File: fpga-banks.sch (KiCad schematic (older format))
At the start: 52 parts, among them J13 62000311121, Q12 2N7002, Q13 2N7002, Q14 2N7002, Q15 2N7002, Q16 2N7002, U14 XC7A100T-FGG484

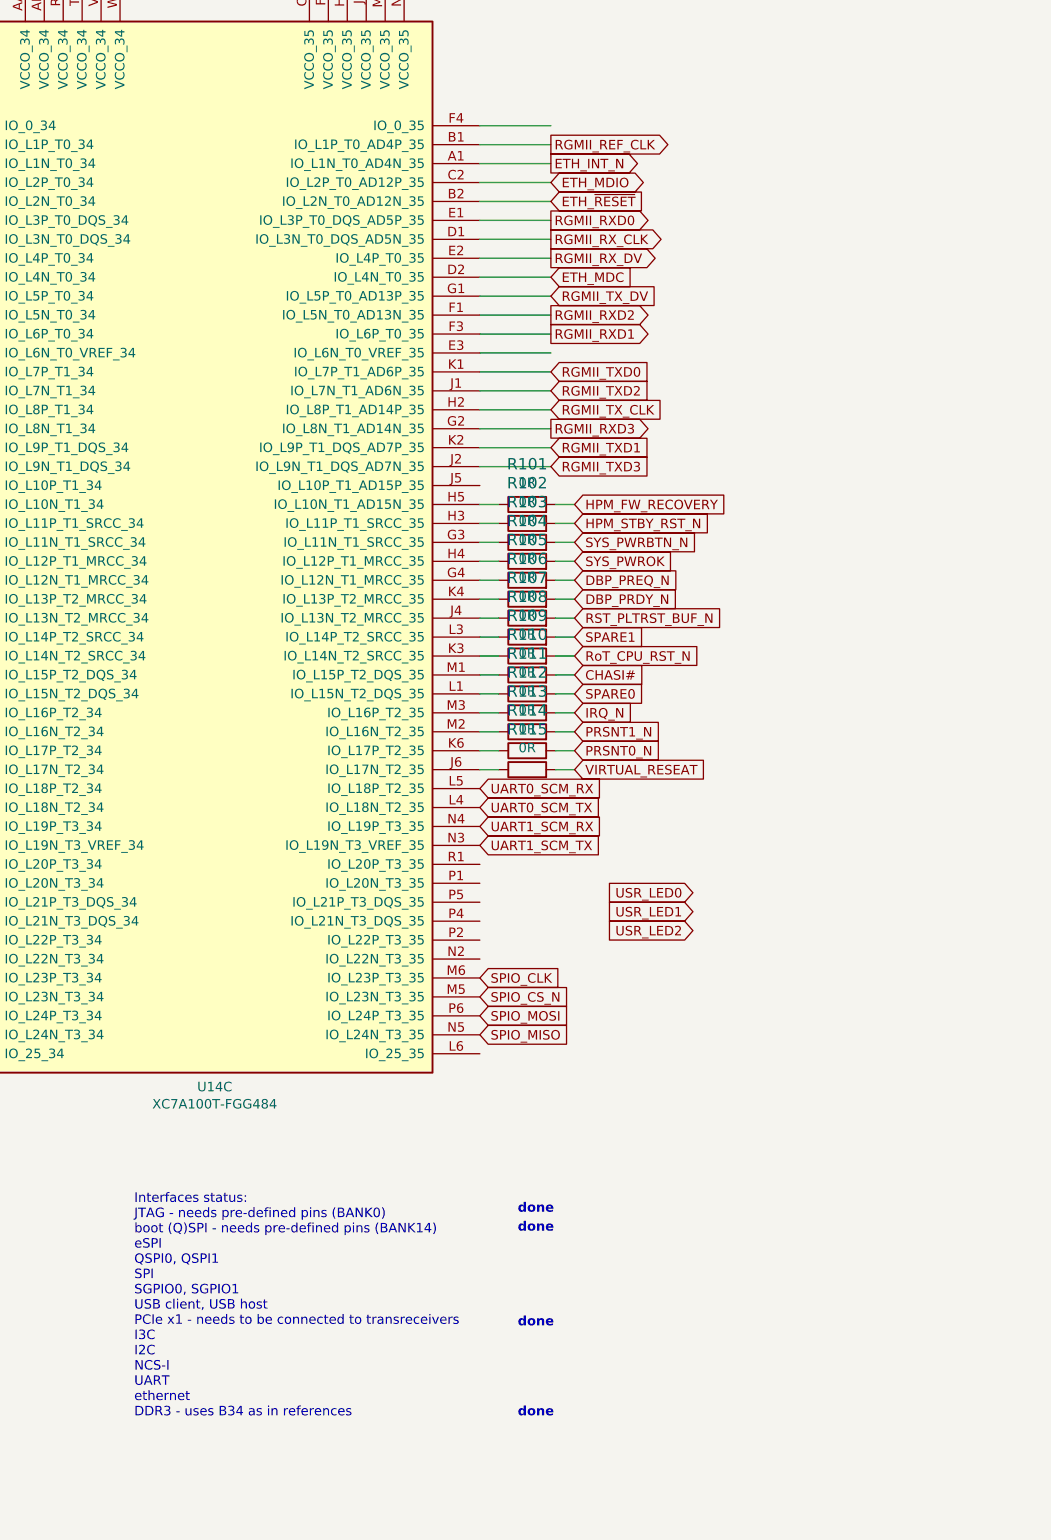
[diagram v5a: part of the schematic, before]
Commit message: Reconnected ethernet
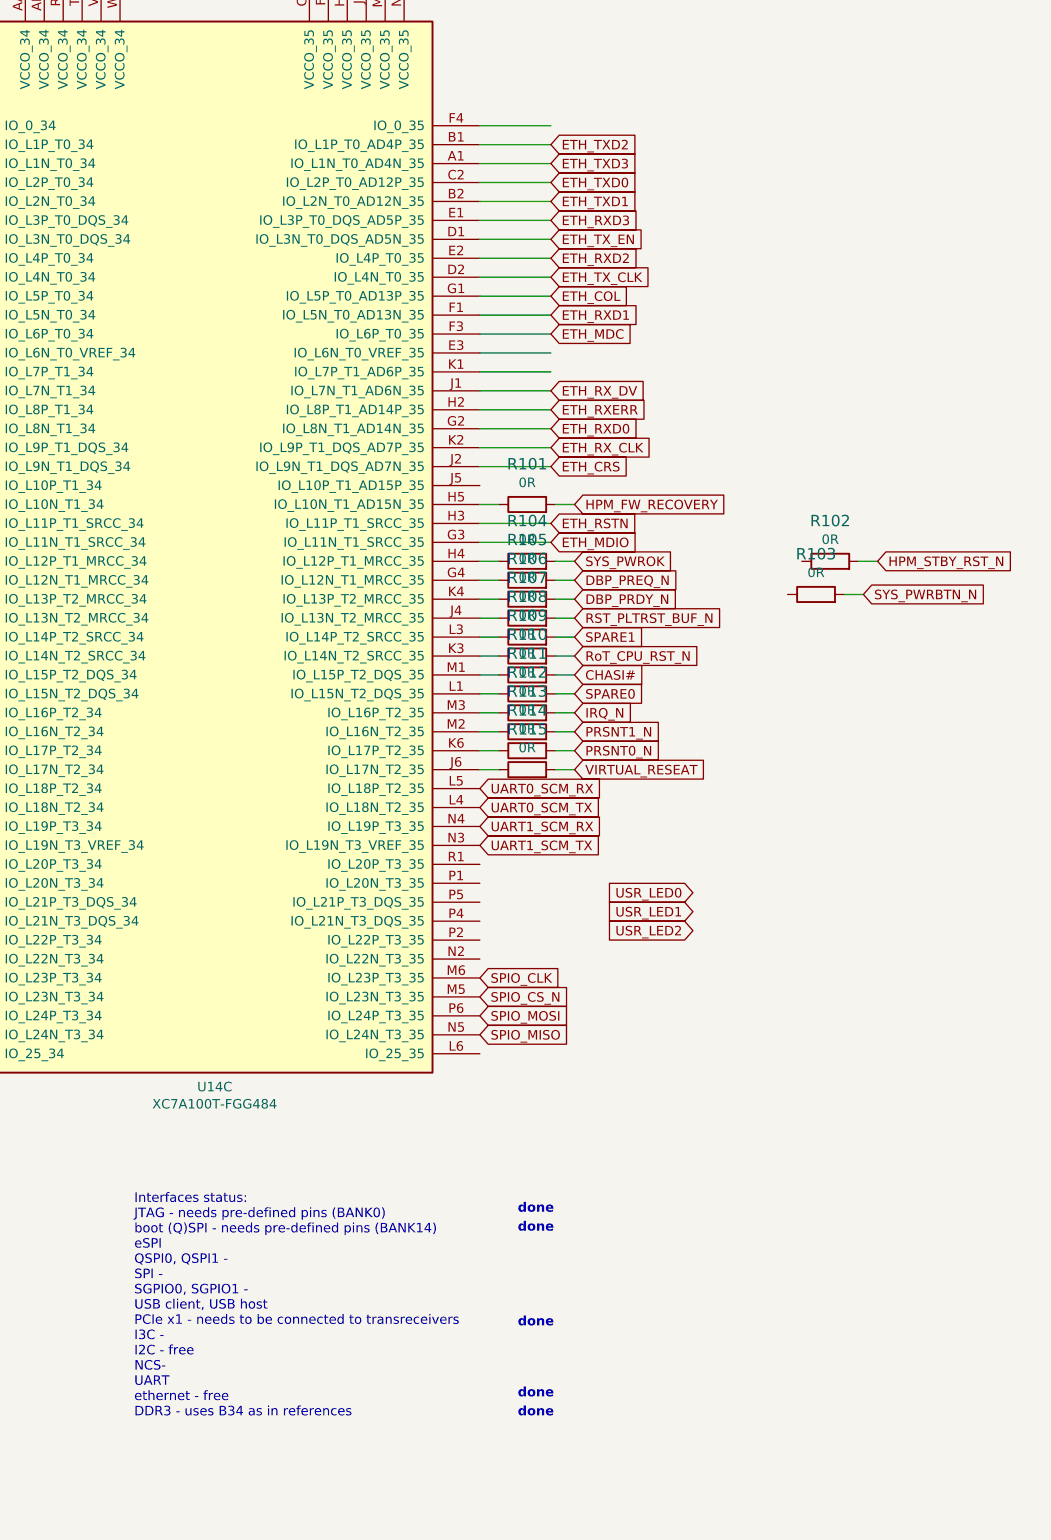
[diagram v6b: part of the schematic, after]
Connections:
- net labels added: ETH_COL, ETH_CRS, ETH_RSTN, ETH_RXD0, ETH_RXD1, ETH_RXD2, ETH_RXD3, ETH_RXERR, ETH_RX_CLK, ETH_RX_DV, ETH_TXD0, ETH_TXD1, ETH_TXD2, ETH_TXD3, ETH_TX_CLK, ETH_TX_EN
- net labels removed: ETH_INT_N, ETH_~RESET, RGMII_REF_CLK, RGMII_RXD0, RGMII_RXD1, RGMII_RXD2, RGMII_RXD3, RGMII_RX_CLK, RGMII_RX_DV, RGMII_TXD0, RGMII_TXD1, RGMII_TXD2, RGMII_TXD3, RGMII_TX_CLK, RGMII_TX_DV
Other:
- note added: "Interfaces status:\nJTAG - needs pre-defined pins (BANK0)\nboot (Q)SPI - needs pre-defined pins (BANK14)\neSPI\nQSPI0, QSPI1 - \nSPI - \nSGPIO0, SGPIO1 - \nUSB client, USB host\nPCIe x1 - needs to be connected to transreceivers\nI3C - \nI2C - free\nNCS-\nUART \nethernet - free\nDDR3 - uses B34 as in references"
- note removed: "Interfaces status:\nJTAG - needs pre-defined pins (BANK0)\nboot (Q)SPI - needs pre-defined pins (BANK14)\neSPI\nQSPI0, QSPI1\nSPI\nSGPIO0, SGPIO1\nUSB client, USB host\nPCIe x1 - needs to be connected to transreceivers\nI3C\nI2C\nNCS-I\nUART\nethernet\nDDR3 - uses B34 as in references"
- moved on the sheet: R102, R103
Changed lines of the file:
@@
 Text GLabel 15300 4000 2    50   Input ~ 0
 HPM_FW_RECOVERY
-Text GLabel 15300 4100 2    50   Input ~ 0
+Text GLabel 16900 4300 2    50   Input ~ 0
 HPM_STBY_RST_N
-Text GLabel 15300 4200 2    50   Input ~ 0
+Text GLabel 16825 4475 2    50   Input ~ 0
 SYS_PWRBTN_N
 Text GLabel 15300 4300 2    50   Input ~ 0
@@
 	0    1    1    0
 $EndComp
-Text GLabel 15175 2400 2    50   Input ~ 0
-ETH_~RESET
-Text GLabel 15175 2200 2    50   Output ~ 0
-ETH_INT_N
-Text GLabel 15175 2100 2    50   Output ~ 0
-RGMII_REF_CLK
-Text GLabel 15175 2300 2    50   BiDi ~ 0
-ETH_MDIO
-Wire Wire Line
-	14800 3800 15175 3800
-Text GLabel 15175 3300 2    50   Input ~ 0
-RGMII_TXD0
-Text GLabel 15175 3700 2    50   Input ~ 0
-RGMII_TXD1
-Text GLabel 15175 3800 2    50   Input ~ 0
-RGMII_TXD3
-Text GLabel 15175 3500 2    50   Input ~ 0
-RGMII_TX_CLK
-Text GLabel 15175 2900 2    50   Input ~ 0
-RGMII_TX_DV
-Text GLabel 15175 3600 2    50   Output ~ 0
-RGMII_RXD3
-Text GLabel 15175 3100 2    50   Output ~ 0
-RGMII_RXD1
-Text GLabel 15175 3400 2    50   Input ~ 0
-RGMII_TXD2
-Text GLabel 15175 3000 2    50   Output ~ 0
-RGMII_RXD2
-Text GLabel 15175 2500 2    50   Output ~ 0
-RGMII_RXD0
-Text GLabel 15175 2700 2    50   Output ~ 0
-RGMII_RX_DV
-Text GLabel 15175 2600 2    50   Output ~ 0
-RGMII_RX_CLK
-Text GLabel 15175 2800 2    50   Input ~ 0
-ETH_MDC
+Wire Wire Line
+	14800 4100 15175 4100
 Wire Wire Line
 	9825 5150 9500 5150
@@
 L artix-dc-scm:R_0R_0402 R102
 U 1 1 61547192
-P 15050 4100
-F 0 "R102" H 15050 4313 60  0000 C CNN
-F 1 "R_0R_0402" H 15050 3950 60  0001 C CNN
-F 2 "artix-dc-scm-footprints:0402-res" H 15250 4300 60  0001 L CNN
-F 3 "" H 15050 4100 50  0001 C CNN
-F 4 "PANASONIC" H 15250 4500 60  0001 L CNN "Manufacturer"
-F 5 "ERJ2GE0R00X" H 15250 4400 60  0001 L CNN "MPN"
-F 6 "0R" H 15050 4215 50  0000 C CNN "Val"
-	1    15050 4100
+P 16650 4300
+F 0 "R102" H 16650 4513 60  0000 C CNN
+F 1 "R_0R_0402" H 16650 4150 60  0001 C CNN
+F 2 "artix-dc-scm-footprints:0402-res" H 16850 4500 60  0001 L CNN
+F 3 "" H 16650 4300 50  0001 C CNN
+F 4 "PANASONIC" H 16850 4700 60  0001 L CNN "Manufacturer"
+F 5 "ERJ2GE0R00X" H 16850 4600 60  0001 L CNN "MPN"
+F 6 "0R" H 16650 4415 50  0000 C CNN "Val"
+	1    16650 4300
 	1    0    0    -1
 $EndComp
@@
 L artix-dc-scm:R_0R_0402 R103
 U 1 1 615497A8
-P 15050 4200
-F 0 "R103" H 15050 4413 60  0000 C CNN
-F 1 "R_0R_0402" H 15050 4050 60  0001 C CNN
-F 2 "artix-dc-scm-footprints:0402-res" H 15250 4400 60  0001 L CNN
-F 3 "" H 15050 4200 50  0001 C CNN
-F 4 "PANASONIC" H 15250 4600 60  0001 L CNN "Manufacturer"
-F 5 "ERJ2GE0R00X" H 15250 4500 60  0001 L CNN "MPN"
-F 6 "0R" H 15050 4315 50  0000 C CNN "Val"
-	1    15050 4200
+P 16575 4475
+F 0 "R103" H 16575 4688 60  0000 C CNN
+F 1 "R_0R_0402" H 16575 4325 60  0001 C CNN
+F 2 "artix-dc-scm-footprints:0402-res" H 16775 4675 60  0001 L CNN
+F 3 "" H 16575 4475 50  0001 C CNN
+F 4 "PANASONIC" H 16775 4875 60  0001 L CNN "Manufacturer"
+F 5 "ERJ2GE0R00X" H 16775 4775 60  0001 L CNN "MPN"
+F 6 "0R" H 16575 4590 50  0000 C CNN "Val"
+	1    16575 4475
 	1    0    0    -1
 $EndComp
@@
 	14800 4000 14900 4000
 Wire Wire Line
-	14800 4100 14900 4100
-Wire Wire Line
-	14800 4200 14900 4200
-Wire Wire Line
 	14800 4300 14900 4300
 Wire Wire Line
@@
 	15200 4000 15300 4000
 Wire Wire Line
-	15200 4100 15300 4100
-Wire Wire Line
-	15200 4200 15300 4200
+	16800 4300 16900 4300
+Wire Wire Line
+	16725 4475 16825 4475
 Wire Wire Line
 	15200 4300 15300 4300
@@
 GPX_USB2
 Text Notes 12975 8825 0    50   ~ 0
-Interfaces status:\nJTAG - needs pre-defined pins (BANK0)\nboot (Q)SPI - needs pre-defined pins (BANK14)\neSPI\nQSPI0, QSPI1\nSPI\nSGPIO0, SGPIO1\nUSB client, USB host\nPCIe x1 - needs to be connected to transreceivers\nI3C\nI2C\nNCS-I\nUART\nethernet\nDDR3 - uses B34 as in references
+Interfaces status:\nJTAG - needs pre-defined pins (BANK0)\nboot (Q)SPI - needs pre-defined pins (BANK14)\neSPI\nQSPI0, QSPI1 - \nSPI - \nSGPIO0, SGPIO1 - \nUSB client, USB host\nPCIe x1 - needs to be connected to transreceivers\nI3C - \nI2C - free\nNCS-\nUART \nethernet - free\nDDR3 - uses B34 as in references
 Text Notes 15000 7750 0    50   ~ 10
 done
@@
 Text Notes 15000 8825 0    50   ~ 10
 done
+Text GLabel 15175 2300 2    50   Input ~ 0
+ETH_TXD0
+Text GLabel 15175 2400 2    50   Input ~ 0
+ETH_TXD1
+Text GLabel 15175 2100 2    50   Input ~ 0
+ETH_TXD2
+Text GLabel 15175 2200 2    50   Input ~ 0
+ETH_TXD3
+Text GLabel 15175 2800 2    50   Input ~ 0
+ETH_TX_CLK
+Text GLabel 15175 2600 2    50   Input ~ 0
+ETH_TX_EN
+Text GLabel 15175 3600 2    50   Input ~ 0
+ETH_RXD0
+Text GLabel 15175 3000 2    50   Input ~ 0
+ETH_RXD1
+Text GLabel 15175 2700 2    50   Input ~ 0
+ETH_RXD2
+Text GLabel 15175 2500 2    50   Input ~ 0
+ETH_RXD3
+Text GLabel 15175 3700 2    50   Input ~ 0
+ETH_RX_CLK
+Text GLabel 15175 3400 2    50   Input ~ 0
+ETH_RX_DV
+Text GLabel 15175 3500 2    50   Input ~ 0
+ETH_RXERR
+Text GLabel 15175 2900 2    50   Input ~ 0
+ETH_COL
+Text GLabel 15175 3800 2    50   Input ~ 0
+ETH_CRS
+Text GLabel 15175 3100 2    50   Input ~ 0
+ETH_MDC
+Text GLabel 15175 4200 2    50   Input ~ 0
+ETH_MDIO
+Text GLabel 15175 4100 2    50   Input ~ 0
+ETH_RSTN
+Wire Wire Line
+	14800 4200 15175 4200
+Wire Wire Line
+	14800 3800 15175 3800
+Text Notes 15000 8725 0    50   ~ 10
+done
 $EndSCHEMATC

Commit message: Reconnected USB
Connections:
- net labels added: INT_USB
- net labels removed: USB1_~RXF, USB1_~TXE
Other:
- note added: "Interfaces status:\nJTAG - needs pre-defined pins (BANK0)\nboot (Q)SPI - needs pre-defined pins (BANK14)\neSPI\nQSPI0, QSPI1 - \nSPI - \nSGPIO0, SGPIO1 - \nUSB client, USB host - free\nPCIe x1 - needs to be connected to transreceivers\nI3C - \nI2C - free\nNCS-\nUART \nethernet - free\nDDR3 - uses B34 as in references"
- note removed: "Interfaces status:\nJTAG - needs pre-defined pins (BANK0)\nboot (Q)SPI - needs pre-defined pins (BANK14)\neSPI\nQSPI0, QSPI1 - \nSPI - \nSGPIO0, SGPIO1 - \nUSB client, USB host\nPCIe x1 - needs to be connected to transreceivers\nI3C - \nI2C - free\nNCS-\nUART \nethernet - free\nDDR3 - uses B34 as in references"
- moved on the sheet: R101, R103, R104, R105, R106, R107, R108, R109, R110, R111, R112, R113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

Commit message: Connected eMMC
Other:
- note added: "Interfaces status:\nJTAG - needs pre-defined pins (BANK0)\nboot (Q)SPI - needs pre-defined pins (BANK14)\neSPI\nQSPI0, QSPI1 - \nSPI - \nSGPIO0, SGPIO1 - \nUSB client, USB host - free\nPCIe x1 - needs to be connected to transreceivers\nI3C - \nI2C - free\nNCSI-\nUART \nethernet - free\nDDR3 - uses B34 as in references\neMMC - free"
- note removed: "Interfaces status:\nJTAG - needs pre-defined pins (BANK0)\nboot (Q)SPI - needs pre-defined pins (BANK14)\neSPI\nQSPI0, QSPI1 - \nSPI - \nSGPIO0, SGPIO1 - \nUSB client, USB host - free\nPCIe x1 - needs to be connected to transreceivers\nI3C - \nI2C - free\nNCS-\nUART \nethernet - free\nDDR3 - uses B34 as in references"
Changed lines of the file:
@@
 Wire Wire Line
 	11600 2500 12000 2500
-Text GLabel 9825 6250 2    50   Input ~ 0
+Text GLabel 10725 150  2    50   Input ~ 0
 USB1_DN
-Text GLabel 9825 5950 2    50   Input ~ 0
+Text GLabel 10725 -150 2    50   Input ~ 0
 USB2_DP
-Text GLabel 9825 6050 2    50   Input ~ 0
+Text GLabel 10725 -50  2    50   Input ~ 0
 USB2_DN
-Text GLabel 9825 5750 2    50   Input ~ 0
+Text GLabel 10725 -350 2    50   Input ~ 0
 SGPIO0_DI
-Text GLabel 9825 5650 2    50   Input ~ 0
+Text GLabel 10725 -450 2    50   Input ~ 0
 SGPIO0_DO
-Text GLabel 9825 4850 2    50   Input ~ 0
+Text GLabel 10725 -1250 2    50   Input ~ 0
 SGPIO0_LD
-Text GLabel 9825 5850 2    50   Input ~ 0
+Text GLabel 10725 -250 2    50   Input ~ 0
 SGPIO1_DI
-Text GLabel 9825 4750 2    50   Input ~ 0
+Text GLabel 10725 -1350 2    50   Input ~ 0
 SGPIO1_DO
-Text GLabel 9825 5150 2    50   Input ~ 0
+Text GLabel 10725 -950 2    50   Input ~ 0
 SGPIO1_LD
-Text GLabel 9825 5450 2    50   Input ~ 0
+Text GLabel 10725 -650 2    50   Input ~ 0
 SGPIO_RESET_N
-Text GLabel 9825 5250 2    50   Input ~ 0
+Text GLabel 10725 -850 2    50   Input ~ 0
 SGPIO_INTR_N
 Text GLabel 950  3400 2    50   Input ~ 0
@@
 Wire Wire Line
 	9825 5150 9500 5150
-Text GLabel 9825 6150 2    50   Input ~ 0
+Text GLabel 10725 50   2    50   Input ~ 0
 USB1_DP
 Wire Wire Line
@@
 Wire Wire Line
 	6375 3650 6700 3650
-Text GLabel 9825 6350 2    50   Input ~ 0
+Text GLabel 10725 250  2    50   Input ~ 0
 QSPI1_D1
-Text GLabel 9825 6450 2    50   Input ~ 0
+Text GLabel 10725 350  2    50   Input ~ 0
 QSPI1_D3
-Text GLabel 9825 6650 2    50   Input ~ 0
+Text GLabel 10725 550  2    50   Input ~ 0
 QSPI1_D2
-Text GLabel 9825 6550 2    50   Input ~ 0
+Text GLabel 10725 450  2    50   Input ~ 0
 QSPI1_D0
-Text GLabel 9825 6850 2    50   Input ~ 0
+Text GLabel 10725 750  2    50   Input ~ 0
 QSPI1_CLK
-Text GLabel 9825 6950 2    50   Input ~ 0
+Text GLabel 10725 850  2    50   Input ~ 0
 QSPI1_CS_N
 Text GLabel 9600 -1625 2    50   Input ~ 0
@@
 Text GLabel 11600 4400 0    50   Output ~ 0
 DDR3_A14
-Text GLabel 1575 7600 2    50   Input ~ 0
+Text GLabel 9825 6050 2    50   Input ~ 0
 MMC_DAT0
-Text GLabel 1575 7700 2    50   Input ~ 0
+Text GLabel 9825 6250 2    50   Input ~ 0
 MMC_DAT1
-Text GLabel 1575 7800 2    50   Input ~ 0
+Text GLabel 9825 6150 2    50   Input ~ 0
 MMC_DAT2
-Text GLabel 1575 7900 2    50   Input ~ 0
+Text GLabel 9825 6450 2    50   Input ~ 0
 MMC_DAT3
-Text GLabel 1575 8000 2    50   Input ~ 0
+Text GLabel 9800 5950 2    50   Input ~ 0
 MMC_DAT4
-Text GLabel 1575 8100 2    50   Input ~ 0
+Text GLabel 9825 6650 2    50   Input ~ 0
 MMC_DAT5
-Text GLabel 1575 8200 2    50   Input ~ 0
+Text GLabel 9825 5250 2    50   Input ~ 0
 MMC_DAT6
-Text GLabel 1575 8300 2    50   Input ~ 0
+Text GLabel 9825 5150 2    50   Input ~ 0
 MMC_DAT7
-Text GLabel 1575 8500 2    50   Input ~ 0
+Text GLabel 9825 5750 2    50   Input ~ 0
 MMC_CMD
-Text GLabel 1575 8600 2    50   Input ~ 0
+Text GLabel 9825 5850 2    50   Input ~ 0
 MMC_CLK
-Text GLabel 1575 8800 2    50   Input ~ 0
+Text GLabel 9825 6550 2    50   Input ~ 0
 MMC_RSTN
-Text GLabel 9825 5050 2    50   Input ~ 0
+Text GLabel 10725 -1050 2    50   Input ~ 0
 SGPIO0_CLK
 Wire Wire Line
@@
 Text GLabel 1550 9650 2    50   Input ~ 0
 NCSI_RXD1
-Text GLabel 9825 5350 2    50   Input ~ 0
+Text GLabel 10725 -750 2    50   Input ~ 0
 RSVD2
-Text Notes 10175 5400 0    50   ~ 0
+Text Notes 11075 -700 0    50   ~ 0
 SGPIO1_CLK
 Text GLabel 5025 2150 2    50   Input ~ 0
@@
 Text GLabel 9875 4150 2    50   Input ~ 0
 GPX_USB2
-Text Notes 12975 8825 0    50   ~ 0
-Interfaces status:\nJTAG - needs pre-defined pins (BANK0)\nboot (Q)SPI - needs pre-defined pins (BANK14)\neSPI\nQSPI0, QSPI1 - \nSPI - \nSGPIO0, SGPIO1 - \nUSB client, USB host - free\nPCIe x1 - needs to be connected to transreceivers\nI3C - \nI2C - free\nNCS-\nUART \nethernet - free\nDDR3 - uses B34 as in references
+Text Notes 13100 8900 0    50   ~ 0
+Interfaces status:\nJTAG - needs pre-defined pins (BANK0)\nboot (Q)SPI - needs pre-defined pins (BANK14)\neSPI\nQSPI0, QSPI1 - \nSPI - \nSGPIO0, SGPIO1 - \nUSB client, USB host - free\nPCIe x1 - needs to be connected to transreceivers\nI3C - \nI2C - free\nNCSI-\nUART \nethernet - free\nDDR3 - uses B34 as in references\neMMC - free
 Text Notes 15000 7750 0    50   ~ 10
 done
@@
 Wire Wire Line
 	14800 3800 15175 3800
-Text Notes 15000 8725 0    50   ~ 10
+Text Notes 15000 8750 0    50   ~ 10
 done
 Text GLabel 9875 4250 2    50   Input ~ 0
@@
 Text Notes 15000 8275 0    50   ~ 10
 done
+Text Notes 15000 8900 0    50   ~ 10
+done
 $EndSCHEMATC
